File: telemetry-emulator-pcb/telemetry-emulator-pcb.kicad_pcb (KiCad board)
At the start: 2 copper layers, 100 x 50 mm, 56 parts, among them IC1 ATmega328P, IC2 MCP2515, IC3 MCP2551, J1 USB, J2 RX_TX, J3 GPIO, J4 CAN_TERM, J5 V_INT, J6 UART, J7 CAN, J8 CAN, J9 CAN, Q1 BSS138, Q2 BSS138, U1 CH340C, Y1 16MHz, Y2 8MHz

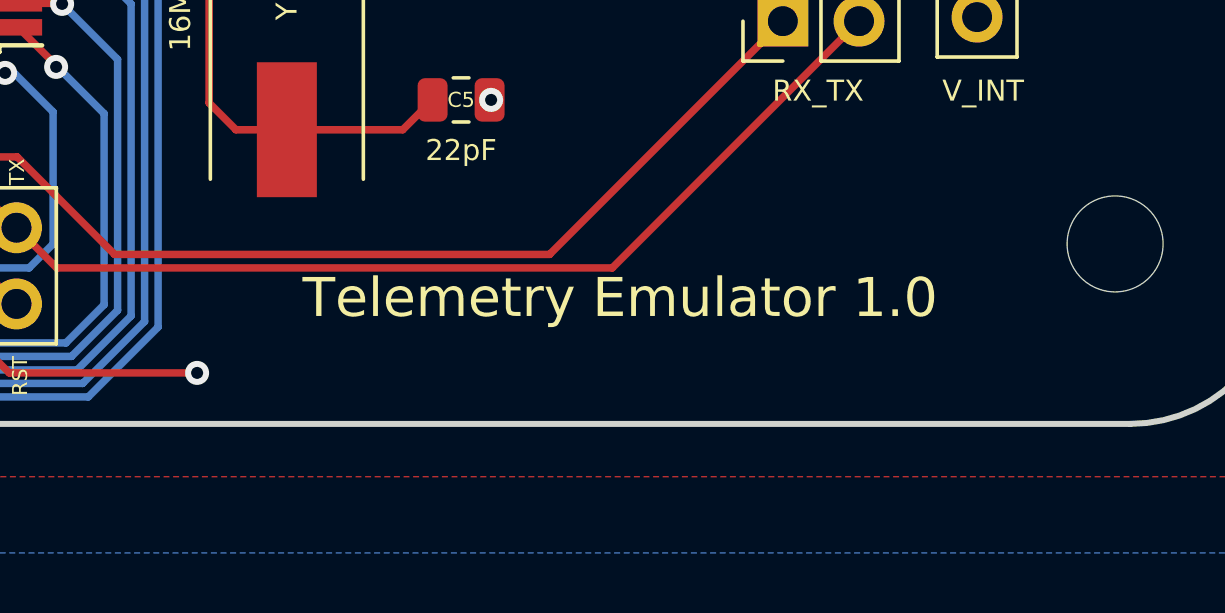
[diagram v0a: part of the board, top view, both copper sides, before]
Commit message: makes supermilage logo a bit smaller
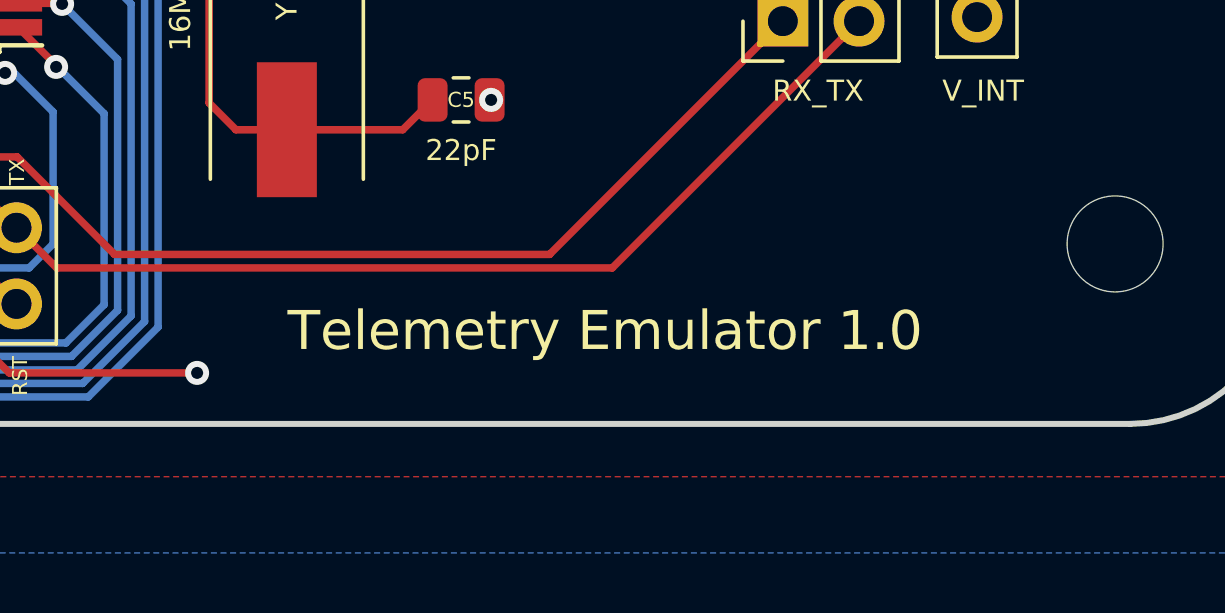
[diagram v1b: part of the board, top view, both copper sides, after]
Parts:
- removed the G*** at (111.8, 91.4)
- added G***: LOGO, LOGO, B.Cu at (108.0, 72.2)

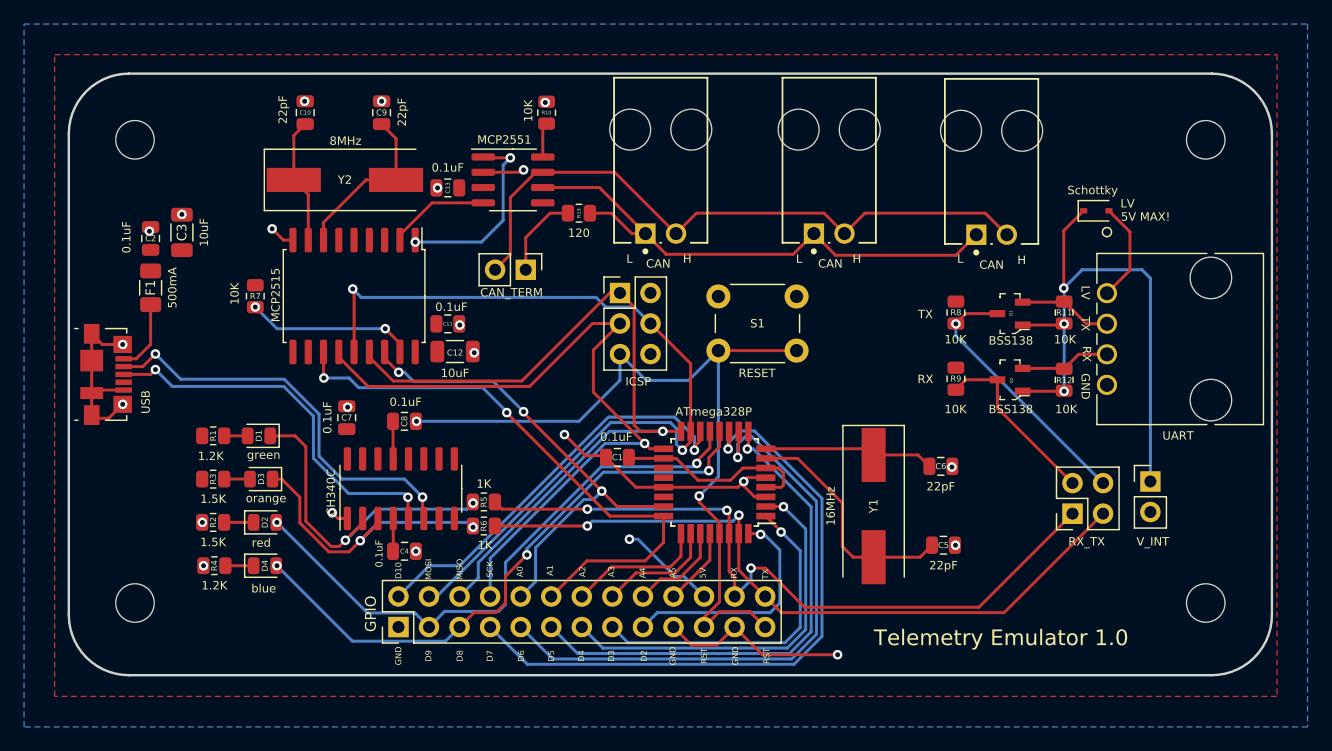
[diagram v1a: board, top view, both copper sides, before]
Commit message: Fixes reset issue
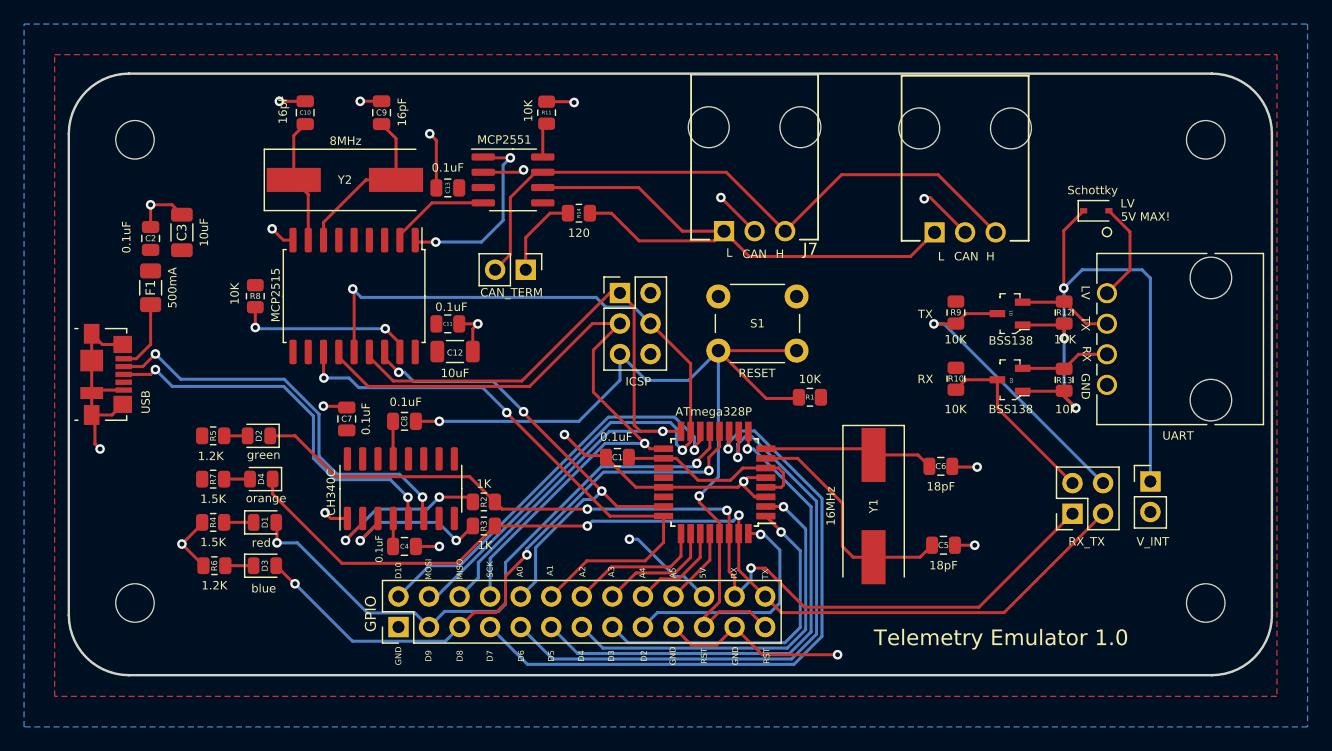
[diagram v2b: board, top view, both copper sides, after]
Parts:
- removed J9: CAN, Molex_SL:molex_sl_1x02_horizontal
- added R1: 10K, Resistor_SMD:R_0805_2012Metric, F.Cu at (146.6, 86.9)
- C10, C9: value 22pF -> 16pF
- C5, C6: value 22pF -> 18pF
- J7, J8: footprint Molex_SL:molex_sl_1x02_horizontal -> Connector_Molex:molex-sl-1x03-horizontal
- moved J8 25.3 mm to (159.5, 67.1)
- moved J7 19.7 mm to (142.0, 67.0)
- moved C4 0.40 mm to (112.9, 99.3)
- moved C7 0.10 mm to (108.1, 88.7)
- renumbered D2 to D1, D1 to D2, D4 to D3, D3 to D4, R9 to R10, R10 to R11, R11 to R12, R12 to R13, R13 to R14, R5 to R2, R6 to R3, R2 to R4, R1 to R5, R4 to R6, R3 to R7, R7 to R8, R8 to R9
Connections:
- D2 pad 1: Net-(D1-Pad1) (its old number) -> RX_USB
- D4 pad 1: Net-(D3-Pad1) (its old number) -> TX_USB
- J7 pad 2: CANH -> Earth
- J8 pad 2: CANH -> Earth
- R2 pad 1: Net-(D1-Pad1) (its old number) -> Net-(R2-Pad1)
- R3 pad 2: Net-(D3-Pad1) (its old number) -> Net-(R3-Pad2)
- U1 pad 2: Net-(D1-Pad1) (its old number) -> Net-(R2-Pad1)
- U1 pad 3: Net-(D3-Pad1) (its old number) -> Net-(R3-Pad2)
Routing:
- net Earth: track 59.9 -> 104.0 mm, vias 22 -> 20
- net Net-(D1-Pad1) (its old number): track 28.2 -> 0.00 mm, vias 2 -> 0
- net Net-(D3-Pad1) (its old number): track 24.1 -> 0.00 mm, vias 2 -> 0
- net TX_USB: track 60.4 -> 84.0 mm
- net RX_USB: track 61.2 -> 82.2 mm
- net Net-(R2-Pad1): track 0.00 -> 14.7 mm, vias 0 -> 2
- net Net-(R3-Pad2): track 0.00 -> 13.6 mm, vias 0 -> 2
- net reset: track 68.1 -> 76.6 mm
- net V_EXT: track 47.8 -> 52.6 mm
- net TX: track 22.1 -> 25.2 mm
- net CANL: track 45.8 -> 48.2 mm
- net D9: track 49.3 -> 50.3 mm
- net Net-(IC2-Pad17): track 14.0 -> 15.0 mm

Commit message: Adds newest drill files
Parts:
- moved R1 4.30 mm to (142.5, 85.6), turned to 180 degrees
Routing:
- net reset: track 76.6 -> 71.8 mm
- net RX_USB: track 82.2 -> 82.7 mm
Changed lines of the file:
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@@
       (effects (font (size 0.7 0.7) (thickness 0.1)))
     )
-    (fp_text value "RESET" (at 3.21 6.378) (layer "F.SilkS")
+    (fp_text value "RESET" (at 8.61 2.478 90) (layer "F.SilkS")
       (effects (font (size 0.7 0.7) (thickness 0.1)))
     )
@@
   )
   (footprint "Resistor_SMD:R_0805_2012Metric" (layer "F.Cu")
-    (at 146.6 86.9)
+    (at 142.5 85.6 180)
     (descr "Resistor SMD 0805 (2012 Metric), square (rectangular) end terminal, IPC_7351 nominal, (Body size source: IPC-SM-782 page 72, https://www.pcb-3d.com/wordpress/wp-content/uploads/ipc-sm-782a_amendment_1_and_2.pdf), generated with kicad-footprint-generator")
     (tags "resistor")
@@
     (fp_line (start -1 -0.625) (end 1 -0.625) (layer "F.Fab") (width 0.1))
     (fp_line (start 1 0.625) (end -1 0.625) (layer "F.Fab") (width 0.1))
-    (pad "1" smd roundrect (at -0.9125 0) (size 1.025 1.4) (layers "F.Cu" "F.Paste" "F.Mask") (roundrect_rratio 0.243902)
+    (pad "1" smd roundrect (at -0.9125 0 180) (size 1.025 1.4) (layers "F.Cu" "F.Paste" "F.Mask") (roundrect_rratio 0.243902)
       (net 1 "+5V") (pintype "passive"))
-    (pad "2" smd roundrect (at 0.9125 0) (size 1.025 1.4) (layers "F.Cu" "F.Paste" "F.Mask") (roundrect_rratio 0.243902)
+    (pad "2" smd roundrect (at 0.9125 0 180) (size 1.025 1.4) (layers "F.Cu" "F.Paste" "F.Mask") (roundrect_rratio 0.243902)
       (net 9 "reset") (pintype "passive"))
     (model "${KICAD6_3DMODEL_DIR}/Resistor_SMD.3dshapes/R_0805_2012Metric.wrl"
@@
   (segment (start 109.3 78.6) (end 128.828 78.6) (width 0.25) (layer "B.Cu") (net 8))
   (segment (start 137.4 95.621) (end 139.084 97.305) (width 0.25) (layer "F.Cu") (net 9))
+  (segment (start 141.5875 85.6) (end 141.568 85.6) (width 0.25) (layer "F.Cu") (net 9))
+  (segment (start 141.568 85.6) (end 138.99 83.022) (width 0.25) (layer "F.Cu") (net 9))
   (segment (start 137.4 95.1045) (end 137.4 95.621) (width 0.25) (layer "F.Cu") (net 9))
   (segment (start 137.8 105.2) (end 137.8 106) (width 0.25) (layer "F.Cu") (net 9))
@@
   (segment (start 139.084 103.916) (end 137.8 105.2) (width 0.25) (layer "F.Cu") (net 9))
   (segment (start 139.084 104.716) (end 137.8 106) (width 0.25) (layer "F.Cu") (net 9))
-  (segment (start 142.968 87) (end 145.5875 87) (width 0.25) (layer "F.Cu") (net 9))
   (segment (start 139.084 97.305) (end 139.084 98.23) (width 0.25) (layer "F.Cu") (net 9))
-  (segment (start 145.5875 87) (end 145.6875 86.9) (width 0.25) (layer "F.Cu") (net 9))
   (segment (start 139.084 98.23) (end 139.084 103.916) (width 0.25) (layer "F.Cu") (net 9))
   (segment (start 141.596 104.716) (end 142.88 106) (width 0.25) (layer "F.Cu") (net 9))
-  (segment (start 138.99 83.022) (end 142.968 87) (width 0.25) (layer "F.Cu") (net 9))
   (via (at 137.4 95.1045) (size 0.8) (drill 0.4) (layers "F.Cu" "B.Cu") (free) (net 9))
   (via (at 115.8 88.9) (size 0.8) (drill 0.4) (layers "F.Cu" "B.Cu") (free) (net 9))
@@
   (segment (start 134.18 102) (end 132.72 103.46) (width 0.25) (layer "F.Cu") (net 25))
   (segment (start 137.484 98.23) (end 137.484 100.216) (width 0.25) (layer "F.Cu") (net 25))
-  (segment (start 107.2 93.5) (end 118.3125 93.5) (width 0.25) (layer "F.Cu") (net 26))
-  (segment (start 103.806 90.106) (end 107.2 93.5) (width 0.25) (layer "F.Cu") (net 26))
+  (segment (start 104.2 93.5) (end 118.3125 93.5) (width 0.25) (layer "F.Cu") (net 26))
+  (segment (start 101.7375 91.0375) (end 104.2 93.5) (width 0.25) (layer "F.Cu") (net 26))
   (segment (start 160.65 104.35) (end 168.425 96.575) (width 0.25) (layer "F.Cu") (net 26))
   (segment (start 120.4125 95.6) (end 121.0125 96.2) (width 0.25) (layer "F.Cu") (net 26))
   (segment (start 139.884 98.23) (end 139.884 96.484) (width 0.25) (layer "F.Cu") (net 26))
   (segment (start 146.15 104.35) (end 160.65 104.35) (width 0.25) (layer "F.Cu") (net 26))
+  (segment (start 118.3125 93.5) (end 120.4125 95.6) (width 0.25) (layer "F.Cu") (net 26))
+  (segment (start 101.7375 90.106) (end 101.7375 91.0375) (width 0.25) (layer "F.Cu") (net 26))
   (segment (start 139.884 98.23) (end 139.884 101.384) (width 0.25) (layer "F.Cu") (net 26))
   (segment (start 140.34 101.84) (end 140.34 103.46) (width 0.25) (layer "F.Cu") (net 26))
   (segment (start 141.7 101.1) (end 142.9 101.1) (width 0.25) (layer "F.Cu") (net 26))
   (segment (start 139.884 101.384) (end 140.34 101.84) (width 0.25) (layer "F.Cu") (net 26))
-  (segment (start 118.3125 93.5) (end 120.4125 95.6) (width 0.25) (layer "F.Cu") (net 26))
   (segment (start 121.0125 96.2) (end 128.1 96.2) (width 0.25) (layer "F.Cu") (net 26))
   (segment (start 139.884 96.484) (end 139.7 96.3) (width 0.25) (layer "F.Cu") (net 26))
-  (segment (start 101.7375 90.106) (end 103.806 90.106) (width 0.25) (layer "F.Cu") (net 26))
   (segment (start 142.9 101.1) (end 146.15 104.35) (width 0.25) (layer "F.Cu") (net 26))
   (via (at 128.1 96.2) (size 0.8) (drill 0.4) (layers "F.Cu" "B.Cu") (net 26))
@@
   (segment (start 107.7 100.7) (end 117.3125 100.7) (width 0.25) (layer "F.Cu") (net 70))
   (segment (start 101.9375 94.9375) (end 107.7 100.7) (width 0.25) (layer "F.Cu") (net 70))
-  (segment (start 120.4125 97.7875) (end 120.4125 97.6) (width 0.25) (layer "F.Cu") (net 70))
   (segment (start 162.74 104.8) (end 170.965 96.575) (width 0.25) (layer "F.Cu") (net 70))
   (segment (start 142.88 103.46) (end 144.22 104.8) (width 0.25) (layer "F.Cu") (net 70))
